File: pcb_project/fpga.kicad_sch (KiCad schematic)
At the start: 49 parts, among them J2 FTSH-107-01-F-DV-K, Q1 BC857BS, Q2 BC847BPN, SW1 SW_Push, U1 XC7A100T-FTG256

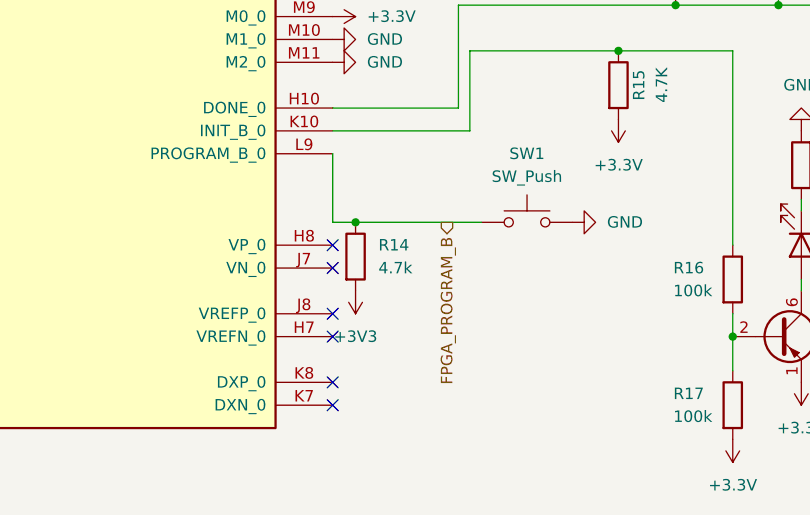
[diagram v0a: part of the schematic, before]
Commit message: Add debounce cap on FPGA reset, add second sram symbol
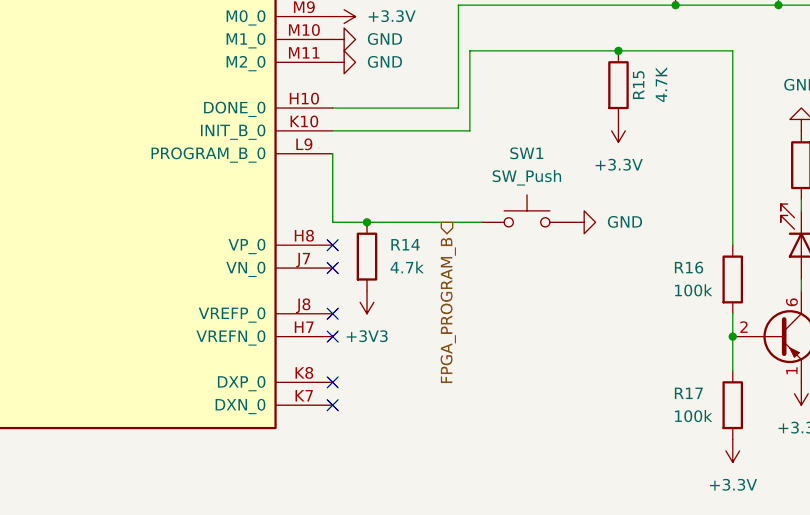
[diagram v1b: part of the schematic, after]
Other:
- moved on the sheet: R14
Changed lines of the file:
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@@
 	)
 	(junction
-		(at 97.79 165.1)
-		(diameter 0)
-		(color 0 0 0 0)
-	)
-	(junction
 		(at 104.14 106.68)
 		(diameter 0)
@@
 	)
 	(junction
+		(at 99.06 165.1)
+		(diameter 0)
+		(color 0 0 0 0)
+	)
+	(junction
 		(at 217.17 121.92)
 		(diameter 0)
@@
 	(wire
 		(pts
-			(xy 95.25 165.1) (xy 97.79 165.1)
+			(xy 95.25 165.1) (xy 99.06 165.1)
 		)
 		(stroke
@@
 	(wire
 		(pts
+			(xy 99.06 165.1) (xy 111.76 165.1)
+		)
+		(stroke
+			(width 0)
+			(type default)
+		)
+	)
+	(wire
+		(pts
 			(xy 267.97 119.38) (xy 267.97 121.92)
 		)
@@
 	(wire
 		(pts
-			(xy 97.79 165.1) (xy 111.76 165.1)
-		)
-		(stroke
-			(width 0)
-			(type default)
-		)
-	)
-	(wire
-		(pts
 			(xy 267.97 139.7) (xy 267.97 142.24)
 		)
@@
 	(symbol
 		(lib_id "power:+3V3")
-		(at 97.79 172.72 180)
+		(at 99.06 172.72 180)
 		(unit 1)
 		(exclude_from_sim no)
@@
 		(fields_autoplaced yes)
 		(property "Reference" "#PWR016"
-			(at 97.79 168.91 0)
+			(at 99.06 168.91 0)
 			(effects
 				(font
@@
 		)
 		(property "Value" "+3V3"
-			(at 97.79 177.8 0)
+			(at 99.06 177.8 0)
 			(effects
 				(font
@@
 		)
 		(property "Footprint" ""
-			(at 97.79 172.72 0)
+			(at 99.06 172.72 0)
 			(effects
 				(font
@@
 		)
 		(property "Datasheet" ""
-			(at 97.79 172.72 0)
+			(at 99.06 172.72 0)
 			(effects
 				(font
@@
 		)
 		(property "Description" "Power symbol creates a global label with name \"+3V3\""
-			(at 97.79 172.72 0)
+			(at 99.06 172.72 0)
 			(effects
 				(font
@@
 	(symbol
 		(lib_id "Device:R")
-		(at 97.79 168.91 0)
+		(at 99.06 168.91 0)
 		(unit 1)
 		(exclude_from_sim no)
@@
 		(fields_autoplaced yes)
 		(property "Reference" "R14"
-			(at 100.33 167.6399 0)
+			(at 101.6 167.6399 0)
 			(effects
 				(font
@@
 		)
 		(property "Value" "4.7k"
-			(at 100.33 170.1799 0)
+			(at 101.6 170.1799 0)
 			(effects
 				(font
@@
 		)
 		(property "Footprint" "Resistor_SMD:R_0805_2012Metric_Pad1.20x1.40mm_HandSolder"
-			(at 96.012 168.91 90)
+			(at 97.282 168.91 90)
 			(effects
 				(font
@@
 		)
 		(property "Datasheet" "~"
-			(at 97.79 168.91 0)
+			(at 99.06 168.91 0)
 			(effects
 				(font
@@
 		)
 		(property "Description" "Resistor"
-			(at 97.79 168.91 0)
+			(at 99.06 168.91 0)
 			(effects
 				(font

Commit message: FPGA decoupler
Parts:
- removed SW1: SW_Push, symbol Switch:SW_Push
- added C78: 100nF, symbol Device:C
- added D12: PESD3V3U1UL, Diode_SMD:D_SOD-882, symbol Diode:PESD3V3U1UL
- added SW4: SW_SPST, symbol Switch:SW_SPST
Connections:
- net FPGA_PROGRAM_B: now also C78.1, D12.1 (K), SW4.1 (A)
- net GND: now also C78.2, D12.2 (A), SW4.2 (B)

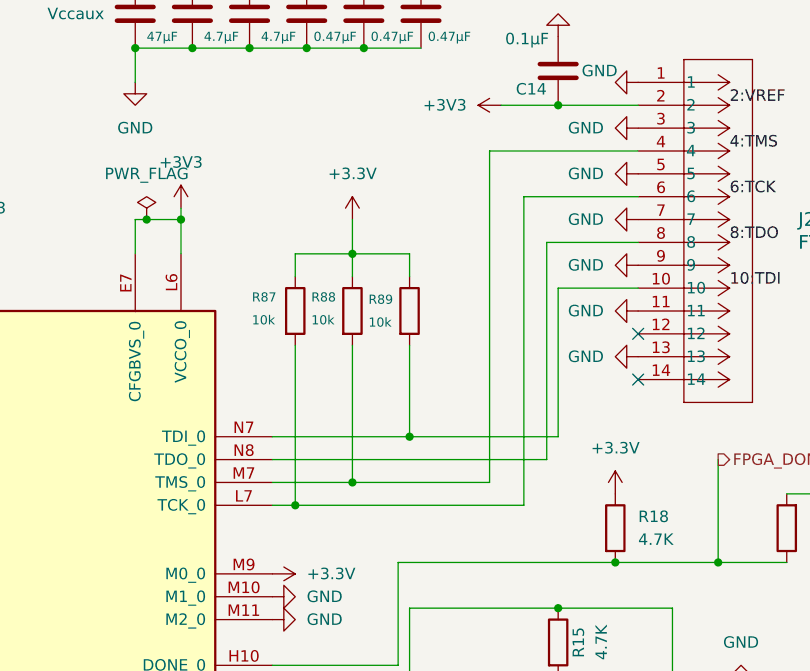
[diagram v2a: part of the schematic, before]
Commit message: Add another SRAM
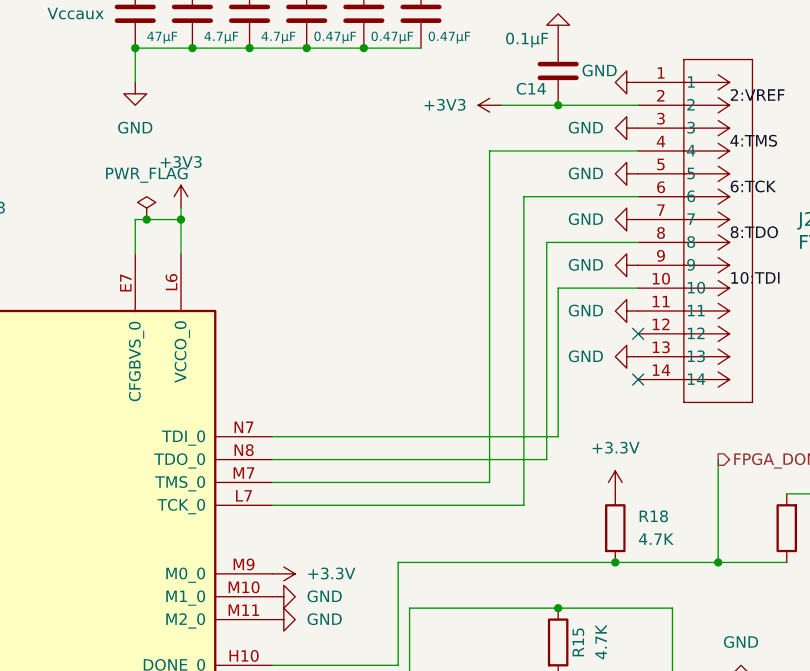
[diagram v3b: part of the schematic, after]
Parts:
- removed R87, R88, R89: 10k, Resistor_SMD:R_0805_2012Metric_Pad1.20x1.40mm_HandSolder, symbol Device:R

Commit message: Fix rest of footprints
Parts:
- C78: footprint (none) -> Capacitor_SMD:C_0603_1608Metric_Pad1.08x0.95mm_HandSolder
- SW4: footprint (none) -> Button_Switch_THT:SW_TH_Tactile_Omron_B3F-100x
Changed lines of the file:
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@@
 			)
 		)
-		(property "Footprint" ""
+		(property "Footprint" "Button_Switch_THT:SW_TH_Tactile_Omron_B3F-100x"
 			(at 121.92 185.42 0)
 			(effects
@@
 			)
 		)
-		(property "Footprint" ""
+		(property "Footprint" "Capacitor_SMD:C_0603_1608Metric_Pad1.08x0.95mm_HandSolder"
 			(at 125.73 164.1348 0)
 			(effects

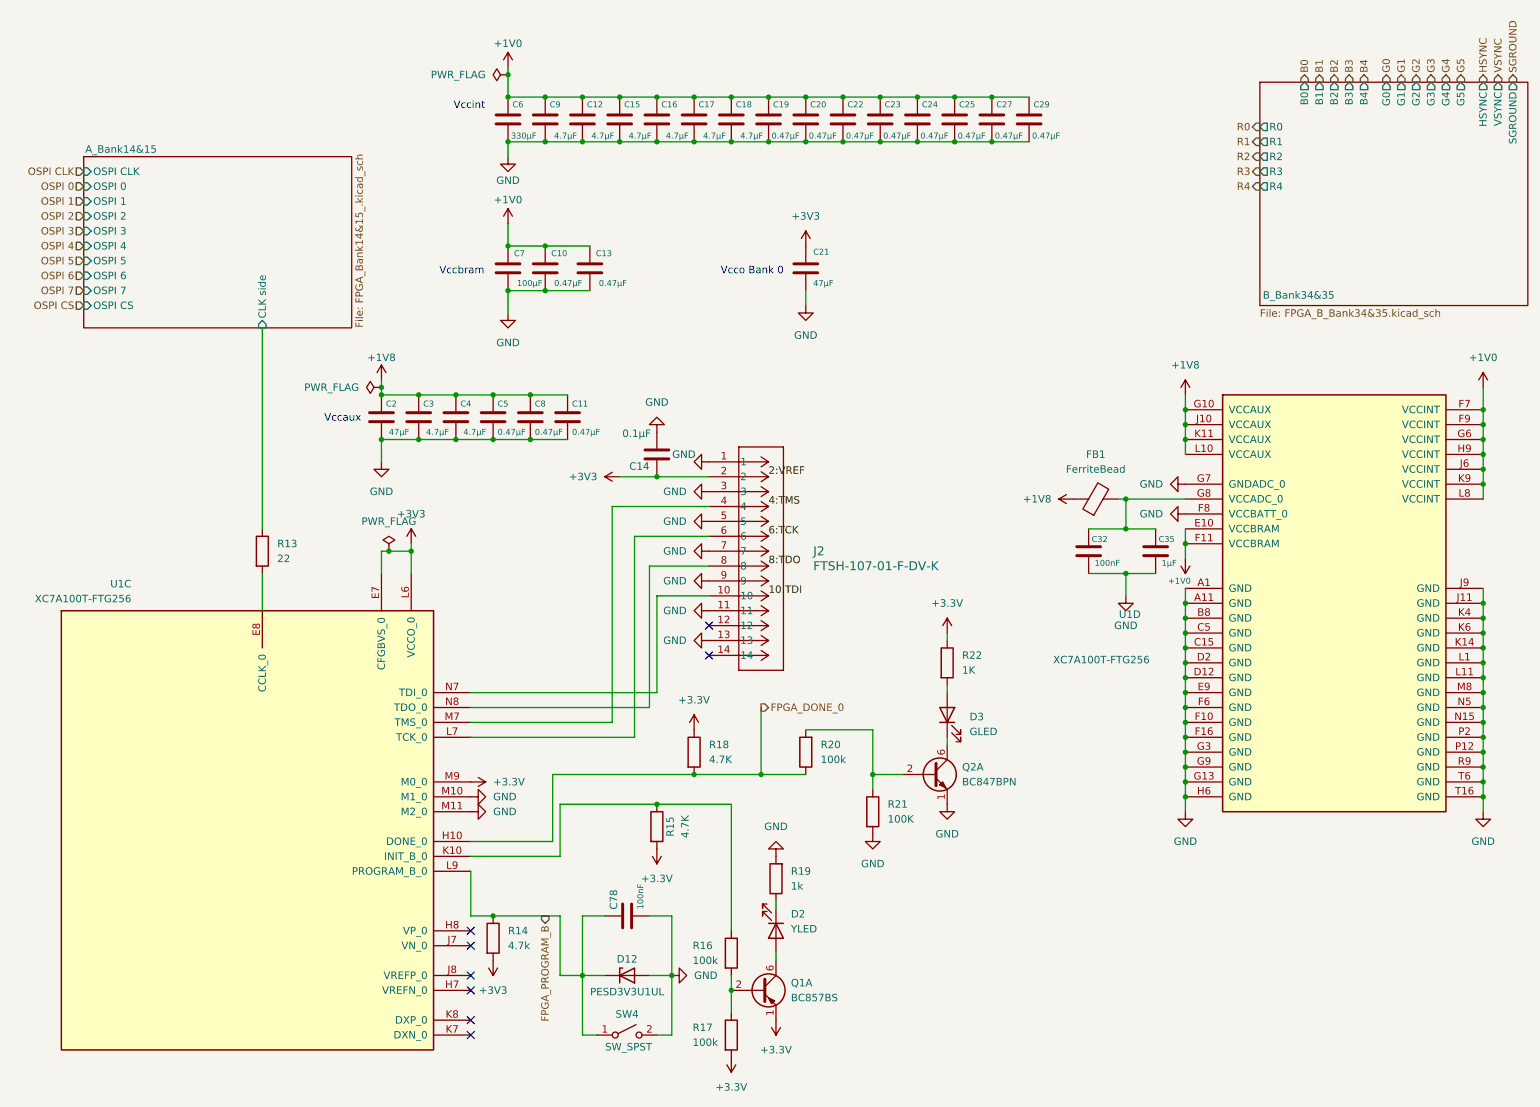
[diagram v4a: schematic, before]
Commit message: Fix ERC errors and update PCB from schematic
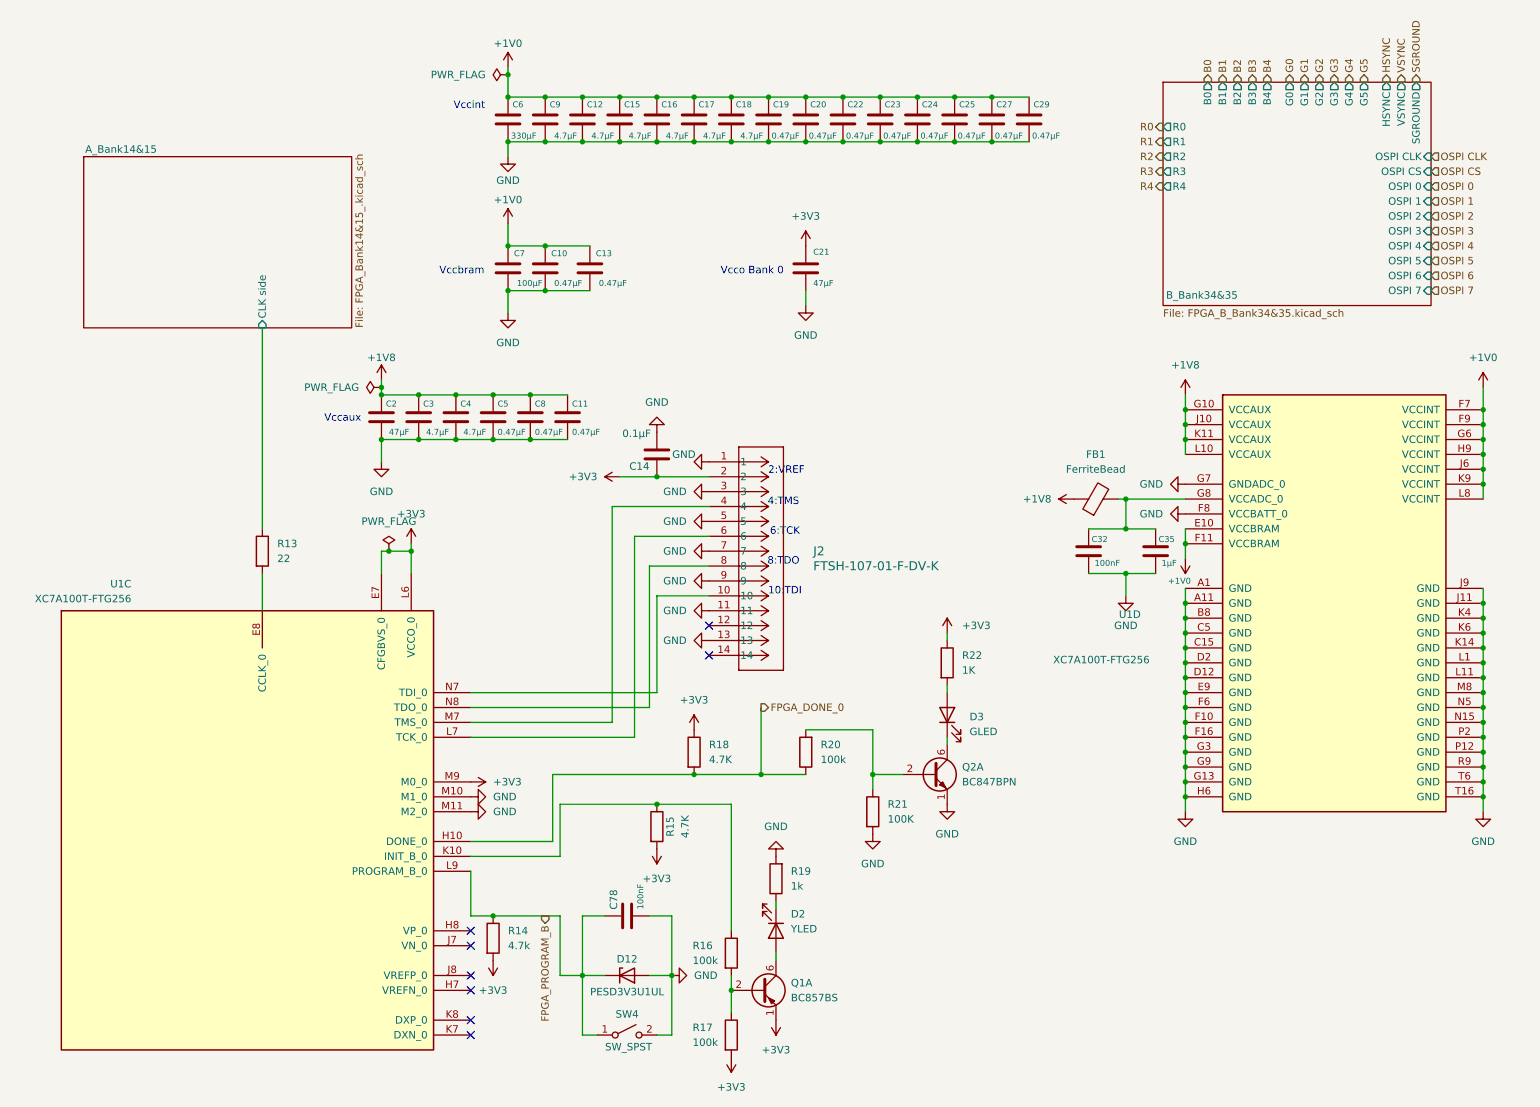
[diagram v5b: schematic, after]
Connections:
- net +3.3V is gone; now on net +3V3: Q1.1 (E1), R15.2, R17.2, R18.1, R22.1, U1.M9 (M0_0)
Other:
- sheet A_Bank14&15 ports: added none; removed OSPI 0, OSPI 1, OSPI 2, OSPI 3, OSPI 4, OSPI 5, OSPI 6, OSPI 7, OSPI CLK, OSPI CS
- sheet B_Bank34&35 ports: added OSPI 0, OSPI 1, OSPI 2, OSPI 3, OSPI 4, OSPI 5, OSPI 6, OSPI 7, OSPI CLK, OSPI CS; removed none
- note added: "10:TDI"
- note added: "2:VREF"
- note added: "4:TMS"
- note added: "6:TCK"
- note added: "8:TDO"

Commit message: Initial FPGA ballout and vga
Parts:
- C10, C11, C13, C19, C20, C22, C23, C24, C25, C27, C29, C5, C8: footprint Capacitor_SMD:C_0805_2012Metric_Pad1.18x1.45mm_HandSolder -> Capacitor_SMD:C_0603_1608Metric_Pad1.08x0.95mm_HandSolder
- C6: footprint Capacitor_SMD:CP_Elec_10x10.5 -> Capacitor_Tantalum_SMD:CP_EIA-7343-31_Kemet-D_HandSolder
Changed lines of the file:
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@@
 			)
 		)
-		(property "Footprint" "Capacitor_SMD:C_0805_2012Metric_Pad1.18x1.45mm_HandSolder"
+		(property "Footprint" "Capacitor_SMD:C_0603_1608Metric_Pad1.08x0.95mm_HandSolder"
 			(at 106.3752 83.82 0)
 			(effects
@@
 			)
 		)
-		(property "Footprint" "Capacitor_SMD:C_0805_2012Metric_Pad1.18x1.45mm_HandSolder"
+		(property "Footprint" "Capacitor_SMD:C_0603_1608Metric_Pad1.08x0.95mm_HandSolder"
 			(at 153.3652 33.02 0)
 			(effects
@@
 			)
 		)
-		(property "Footprint" "Capacitor_SMD:C_0805_2012Metric_Pad1.18x1.45mm_HandSolder"
+		(property "Footprint" "Capacitor_SMD:C_0603_1608Metric_Pad1.08x0.95mm_HandSolder"
 			(at 159.7152 33.02 0)
 			(effects
@@
 			)
 		)
-		(property "Footprint" "Capacitor_SMD:CP_Elec_10x10.5"
+		(property "Footprint" "Capacitor_Tantalum_SMD:CP_EIA-7343-31_Kemet-D_HandSolder"
 			(at 102.5652 33.02 0)
 			(effects
@@
 			)
 		)
-		(property "Footprint" "Capacitor_SMD:C_0805_2012Metric_Pad1.18x1.45mm_HandSolder"
+		(property "Footprint" "Capacitor_SMD:C_0603_1608Metric_Pad1.08x0.95mm_HandSolder"
 			(at 100.0252 83.82 0)
 			(effects
@@
 			)
 		)
-		(property "Footprint" "Capacitor_SMD:C_0805_2012Metric_Pad1.18x1.45mm_HandSolder"
+		(property "Footprint" "Capacitor_SMD:C_0603_1608Metric_Pad1.08x0.95mm_HandSolder"
 			(at 185.1152 33.02 0)
 			(effects
@@
 			)
 		)
-		(property "Footprint" "Capacitor_SMD:C_0805_2012Metric_Pad1.18x1.45mm_HandSolder"
+		(property "Footprint" "Capacitor_SMD:C_0603_1608Metric_Pad1.08x0.95mm_HandSolder"
 			(at 178.7652 33.02 0)
 			(effects
@@
 			)
 		)
-		(property "Footprint" "Capacitor_SMD:C_0805_2012Metric_Pad1.18x1.45mm_HandSolder"
+		(property "Footprint" "Capacitor_SMD:C_0603_1608Metric_Pad1.08x0.95mm_HandSolder"
 			(at 191.4652 33.02 0)
 			(effects
@@
 			)
 		)
-		(property "Footprint" "Capacitor_SMD:C_0805_2012Metric_Pad1.18x1.45mm_HandSolder"
+		(property "Footprint" "Capacitor_SMD:C_0603_1608Metric_Pad1.08x0.95mm_HandSolder"
 			(at 147.0152 33.02 0)
 			(effects
@@
 			)
 		)
-		(property "Footprint" "Capacitor_SMD:C_0805_2012Metric_Pad1.18x1.45mm_HandSolder"
+		(property "Footprint" "Capacitor_SMD:C_0603_1608Metric_Pad1.08x0.95mm_HandSolder"
 			(at 166.0652 33.02 0)
 			(effects
@@
 			)
 		)
-		(property "Footprint" "Capacitor_SMD:C_0805_2012Metric_Pad1.18x1.45mm_HandSolder"
+		(property "Footprint" "Capacitor_SMD:C_0603_1608Metric_Pad1.08x0.95mm_HandSolder"
 			(at 116.5352 58.42 0)
 			(effects
@@
 			)
 		)
-		(property "Footprint" "Capacitor_SMD:C_0805_2012Metric_Pad1.18x1.45mm_HandSolder"
+		(property "Footprint" "Capacitor_SMD:C_0603_1608Metric_Pad1.08x0.95mm_HandSolder"
 			(at 112.7252 83.82 0)
 			(effects
@@
 			)
 		)
-		(property "Footprint" "Capacitor_SMD:C_0805_2012Metric_Pad1.18x1.45mm_HandSolder"
+		(property "Footprint" "Capacitor_SMD:C_0603_1608Metric_Pad1.08x0.95mm_HandSolder"
 			(at 172.4152 33.02 0)
 			(effects
@@
 			)
 		)
-		(property "Footprint" "Capacitor_SMD:C_0805_2012Metric_Pad1.18x1.45mm_HandSolder"
+		(property "Footprint" "Capacitor_SMD:C_0603_1608Metric_Pad1.08x0.95mm_HandSolder"
 			(at 108.9152 58.42 0)
 			(effects

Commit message: Clean up FPGA pins, and other small improvements
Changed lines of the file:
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@@
-	(wire
-		(pts
-			(xy 80.01 106.68) (xy 80.01 102.87)
-		)
-		(stroke
-			(width 0)
-			(type default)
-		)
-	)
 	(wire
 		(pts
@@
 	(wire
 		(pts
+			(xy 81.28 102.87) (xy 85.09 102.87)
+		)
+		(stroke
+			(width 0)
+			(type default)
+		)
+	)
+	(wire
+		(pts
 			(xy 109.22 140.97) (xy 133.35 140.97)
 		)
@@
 	(wire
 		(pts
-			(xy 81.28 102.87) (xy 85.09 102.87)
-		)
-		(stroke
-			(width 0)
-			(type default)
-		)
-	)
-	(wire
-		(pts
 			(xy 267.97 78.74) (xy 267.97 81.28)
 		)
@@
 		)
 		(stroke
+			(width 0)
+			(type default)
+		)
+	)
+	(wire
+		(pts
+			(xy 80.01 102.87) (xy 80.01 106.68)
+		)
+		(stroke
